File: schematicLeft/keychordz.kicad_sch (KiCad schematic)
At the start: 29 parts, among them J1 USB_C_Receptacle_USB2.0, SW1 SW_Push, SW2 SW_Push, SW3 SW_Push, SW4 SW_Push, SW5 SW_Push, SW6 SW_Push, SW7 SW_Push

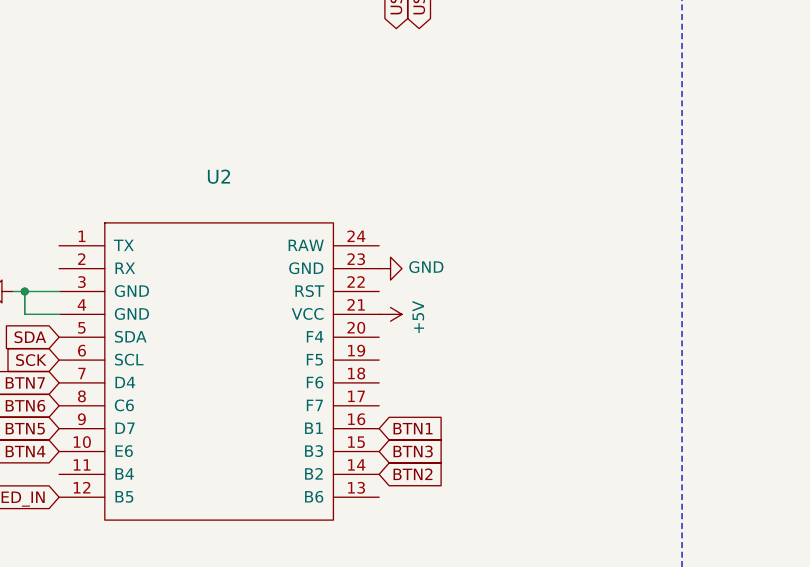
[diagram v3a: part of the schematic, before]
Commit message: fix LED vcc
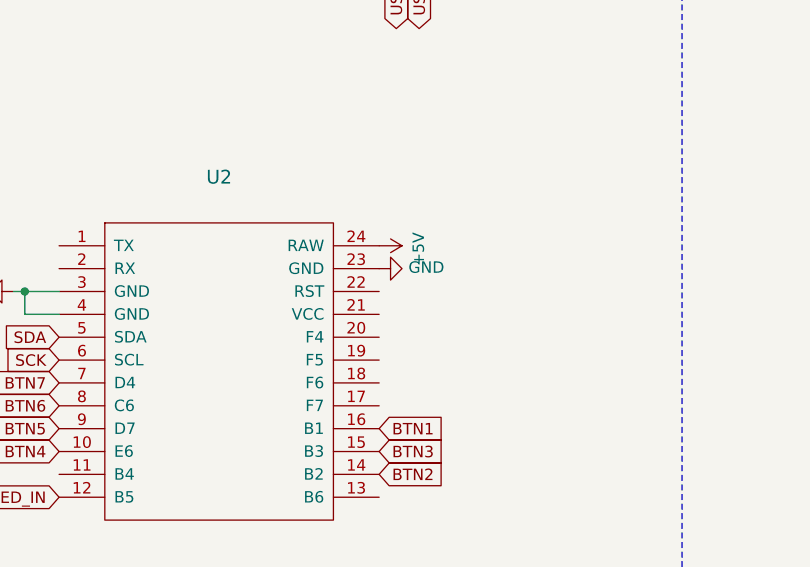
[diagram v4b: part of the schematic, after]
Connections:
- net +5V: now also U2.24 (RAW); no longer U2.21 (VCC)
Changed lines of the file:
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@@
     (pin "4")
   )
-  (symbol (lib_id "power:+5V") (at 175.26 124.46 270) (unit 1)
+  (symbol (lib_id "power:+5V") (at 175.26 116.84 270) (unit 1)
     (in_bom yes) (on_board yes)
-    (property "Reference" "#PWR0111" (id 0) (at 171.45 124.46 0)
+    (property "Reference" "#PWR0111" (id 0) (at 171.45 116.84 0)
       (effects (font (size 1.27 1.27)) hide)
     )
-    (property "Value" "+5V" (id 1) (at 179.6542 124.841 0))
-    (property "Footprint" "" (id 2) (at 175.26 124.46 0)
+    (property "Value" "+5V" (id 1) (at 179.6542 117.221 0))
+    (property "Footprint" "" (id 2) (at 175.26 116.84 0)
       (effects (font (size 1.27 1.27)) hide)
     )
-    (property "Datasheet" "" (id 3) (at 175.26 124.46 0)
+    (property "Datasheet" "" (id 3) (at 175.26 116.84 0)
       (effects (font (size 1.27 1.27)) hide)
     )
